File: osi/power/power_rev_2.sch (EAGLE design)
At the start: 11 parts, among them IC1 UA7805CKCS, IC2 MCP1702

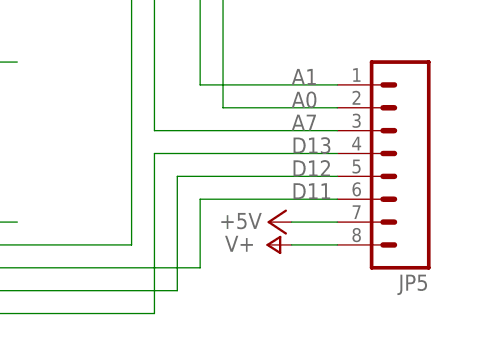
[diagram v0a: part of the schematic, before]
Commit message: moving headers
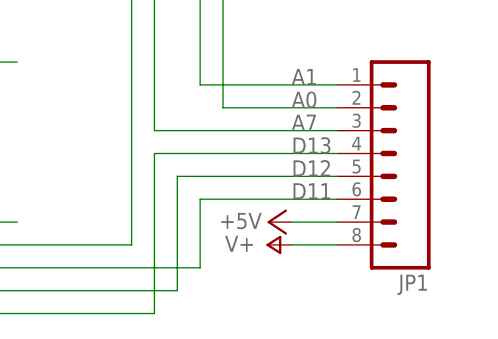
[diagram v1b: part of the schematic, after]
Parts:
- removed JP5: (no value), SparkFun_mod:M081X08
- added JP1: (no value), SparkFun:M081X08
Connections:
- net +5V: now also JP1.7; no longer JP5.7
- net A0: now also JP1.2; no longer JP5.2
- net A1: now also JP1.1; no longer JP5.1
- net A7: now also JP1.3; no longer JP5.3
- net D11: now also JP1.6; no longer JP5.6
- net D12: now also JP1.5; no longer JP5.5
- net D13: now also JP1.4; no longer JP5.4
- net V+: now also JP1.8; no longer JP5.8
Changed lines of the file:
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@@
 <part name="JP6" library="SparkFun" deviceset="M06" device="SIP"/>
 <part name="FRAME1" library="SparkFun_mod" deviceset="FRAME-LETTER" device=""/>
-<part name="JP5" library="SparkFun_mod" deviceset="M08" device="1X08"/>
 <part name="GND4" library="SparkFun" deviceset="GND" device=""/>
 <part name="P+6" library="supply1" deviceset="+5V" device=""/>
@@
 <part name="C2" library="adafruit" deviceset="C-US" device="025-024X044" value="1uF"/>
 <part name="R1" library="adafruit" deviceset="R-US_" device="0204/5" value="1k"/>
+<part name="JP1" library="SparkFun" deviceset="M08" device="1X08"/>
 </parts>
 <sheets>
@@
 <instance part="FRAME1" gate="G$1" x="-73.66" y="-30.48"/>
 <instance part="FRAME1" gate="G$2" x="73.66" y="-30.48"/>
-<instance part="JP5" gate="G$1" x="132.08" y="30.48" rot="R180"/>
 <instance part="GND4" gate="1" x="0" y="48.26"/>
 <instance part="P+6" gate="1" x="27.94" y="71.12" smashed="yes">
@@
 <instance part="C2" gate="G$1" x="27.94" y="55.88"/>
 <instance part="R1" gate="G$1" x="35.56" y="78.74" rot="R90"/>
+<instance part="JP1" gate="G$1" x="132.08" y="30.48" rot="R180"/>
 </instances>
 <busses>
@@
 <net name="V+" class="0">
 <segment>
-<pinref part="JP5" gate="G$1" pin="8"/>
 <pinref part="P+2" gate="1" pin="V+"/>
 <wire x1="127" y1="20.32" x2="121.92" y2="20.32" width="0.1524" layer="91"/>
+<pinref part="JP1" gate="G$1" pin="8"/>
 </segment>
 <segment>
@@
 <wire x1="81.28" y1="71.12" x2="114.3" y2="71.12" width="0.1524" layer="91"/>
 <wire x1="114.3" y1="71.12" x2="114.3" y2="35.56" width="0.1524" layer="91"/>
-<pinref part="JP5" gate="G$1" pin="2"/>
 <wire x1="114.3" y1="35.56" x2="127" y2="35.56" width="0.1524" layer="91"/>
 <label x="121.92" y="35.56" size="1.778" layer="95"/>
+<pinref part="JP1" gate="G$1" pin="2"/>
 </segment>
 </net>
@@
 <net name="+5V" class="0">
 <segment>
-<pinref part="JP5" gate="G$1" pin="7"/>
 <pinref part="P+3" gate="1" pin="+5V"/>
 <wire x1="127" y1="22.86" x2="121.92" y2="22.86" width="0.1524" layer="91"/>
+<pinref part="JP1" gate="G$1" pin="7"/>
 </segment>
 <segment>
@@
 <wire x1="111.76" y1="68.58" x2="111.76" y2="38.1" width="0.1524" layer="91"/>
 <wire x1="111.76" y1="38.1" x2="127" y2="38.1" width="0.1524" layer="91"/>
-<pinref part="JP5" gate="G$1" pin="1"/>
 <label x="121.92" y="38.1" size="1.778" layer="95"/>
+<pinref part="JP1" gate="G$1" pin="1"/>
 </segment>
 </net>
@@
 <wire x1="111.76" y1="17.78" x2="111.76" y2="25.4" width="0.1524" layer="91"/>
 <wire x1="111.76" y1="25.4" x2="127" y2="25.4" width="0.1524" layer="91"/>
-<pinref part="JP5" gate="G$1" pin="6"/>
 <label x="121.92" y="25.4" size="1.778" layer="95"/>
+<pinref part="JP1" gate="G$1" pin="6"/>
 </segment>
 </net>
@@
 <wire x1="81.28" y1="15.24" x2="109.22" y2="15.24" width="0.1524" layer="91"/>
 <wire x1="109.22" y1="15.24" x2="109.22" y2="27.94" width="0.1524" layer="91"/>
-<pinref part="JP5" gate="G$1" pin="5"/>
 <wire x1="109.22" y1="27.94" x2="127" y2="27.94" width="0.1524" layer="91"/>
 <label x="121.92" y="27.94" size="1.778" layer="95"/>
+<pinref part="JP1" gate="G$1" pin="5"/>
 </segment>
 </net>
@@
 <wire x1="81.28" y1="12.7" x2="106.68" y2="12.7" width="0.1524" layer="91"/>
 <wire x1="106.68" y1="12.7" x2="106.68" y2="30.48" width="0.1524" layer="91"/>
-<pinref part="JP5" gate="G$1" pin="4"/>
 <wire x1="106.68" y1="30.48" x2="127" y2="30.48" width="0.1524" layer="91"/>
 <label x="121.92" y="30.48" size="1.778" layer="95"/>
+<pinref part="JP1" gate="G$1" pin="4"/>
 </segment>
 </net>
@@
 <wire x1="81.28" y1="53.34" x2="106.68" y2="53.34" width="0.1524" layer="91"/>
 <wire x1="106.68" y1="53.34" x2="106.68" y2="33.02" width="0.1524" layer="91"/>
-<pinref part="JP5" gate="G$1" pin="3"/>
 <wire x1="106.68" y1="33.02" x2="127" y2="33.02" width="0.1524" layer="91"/>
 <label x="121.92" y="33.02" size="1.778" layer="95"/>
-</segment>
-</net>
+<pinref part="JP1" gate="G$1" pin="3"/>
+</segment>
+</net>
